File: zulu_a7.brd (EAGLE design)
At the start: 61 x 25.4 mm, 183 parts, among them J1 Pmod 2x6, Q1 12MHz 25ppm (FPGA + FT2232HQ), Q2 2N7002, Q3 MBT3904DW1T1, U1 XC7A35T-1CPG236C, U10 93LC46BT-I/SN, U2 FT2232HQ USB-UART/JTAG Bridge, U3 AS4C32M16SB-6TIN, U4 W25Q128JVSIQ, U8 LTC3569EUDC#TRPBF, X1 Molex 105017-0001 Micro-USB-B

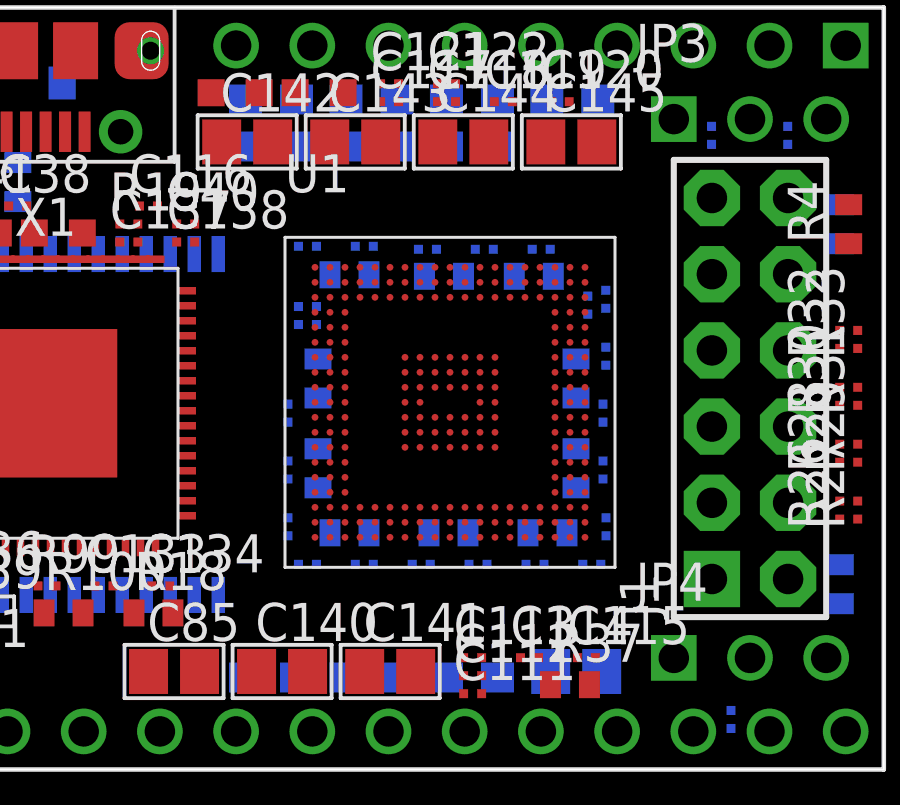
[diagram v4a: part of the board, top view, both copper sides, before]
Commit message: The BGA escape goes in: 1297 wires, 157 vias, DRC clean
First copper on the board. tools/escape.py --apply, run after make_board and
never before -- make_board rewrites <signals> empty, so regenerating from here
throws the escape away and this has to be re-run. That is intended: placement is
the source of truth and the escape is derived from it.

    stage 1  113 power and ground balls ganged on L1: 73 edges, 40 components
    stage 2  54 escapes drop through vias in the 2.00 mm moat
    stage 3  103 escapes leave the package to a fan-out ring at 7.260 mm
             half-width, 103 vias at 0.390 pitch using 40.170 of 58.080 mm

The escape CLOSES: all 47 enclosed ring-1 balls found a lane, every one outward
through ring 0, none needing to come inward through ring 2.

Not one via goes inside the ball field, and the arithmetic for that is worth
keeping in view: at a 0.225 land the four-ball void is 0.4821 across, and 0.090
of clearance leaves 0.3021 for a via land against the board's 0.300. It "fits"
by 0.0021 mm, which is a rounding error and not a fit.

check_board: 1297 wires and 157 vias across 175 signals, all copper on L1, every
wire and via clearing foreign copper by the full 0.090, every wire end landing on
its own net. 0 findings. 52 of 175 signals still carry no copper.

The docstring said stage 1 was all the file did. It has done all three for some
time; it now says so, and says what it does NOT do -- seven ganged components are
stranded (P2, B14, H18, V18 on GND, V6, V9, V11 on VCC3V3) and need a lane each
like a signal, which this pass does not draw.

Co-Authored-By: Claude Opus 5 <noreply@anthropic.com>
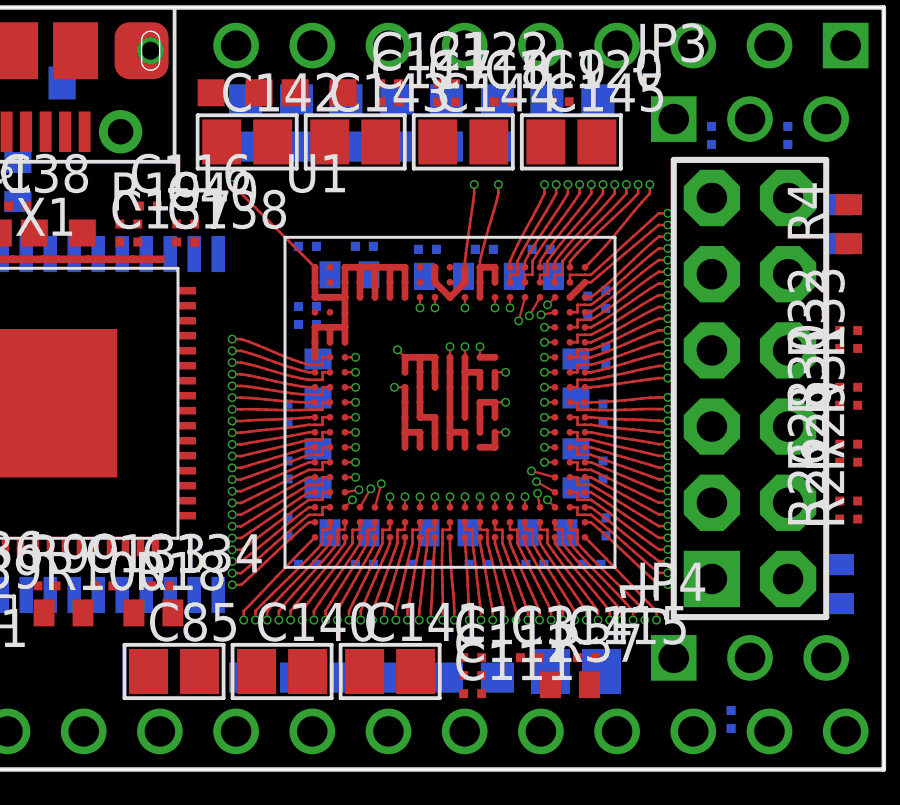
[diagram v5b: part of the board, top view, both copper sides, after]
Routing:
- net GND: track 0.00 -> 72.6 mm, vias 0 -> 19
- net VCC3V3: track 0.00 -> 33.5 mm, vias 0 -> 16
- net GNDADC: track 0.00 -> 4.84 mm, vias 0 -> 1
- net BS0: track 0.00 -> 4.43 mm, vias 0 -> 1
- net CHAN2: track 0.00 -> 4.36 mm, vias 0 -> 1
- net VCC1V0: track 0.00 -> 4.35 mm, vias 0 -> 1
- net CHAN0: track 0.00 -> 4.30 mm, vias 0 -> 1
- net CHAN15: track 0.00 -> 4.24 mm, vias 0 -> 1
- net RAS#: track 0.00 -> 4.24 mm, vias 0 -> 1
- net A0: track 0.00 -> 4.23 mm, vias 0 -> 1
- net JA1: track 0.00 -> 4.23 mm, vias 0 -> 1
- net FLASH-D00: track 0.00 -> 4.19 mm, vias 0 -> 1
- net UART_FT_CTS#: track 0.00 -> 4.17 mm, vias 0 -> 1
- net CHAN18: track 0.00 -> 4.07 mm, vias 0 -> 1
- net WE#: track 0.00 -> 4.06 mm, vias 0 -> 1
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
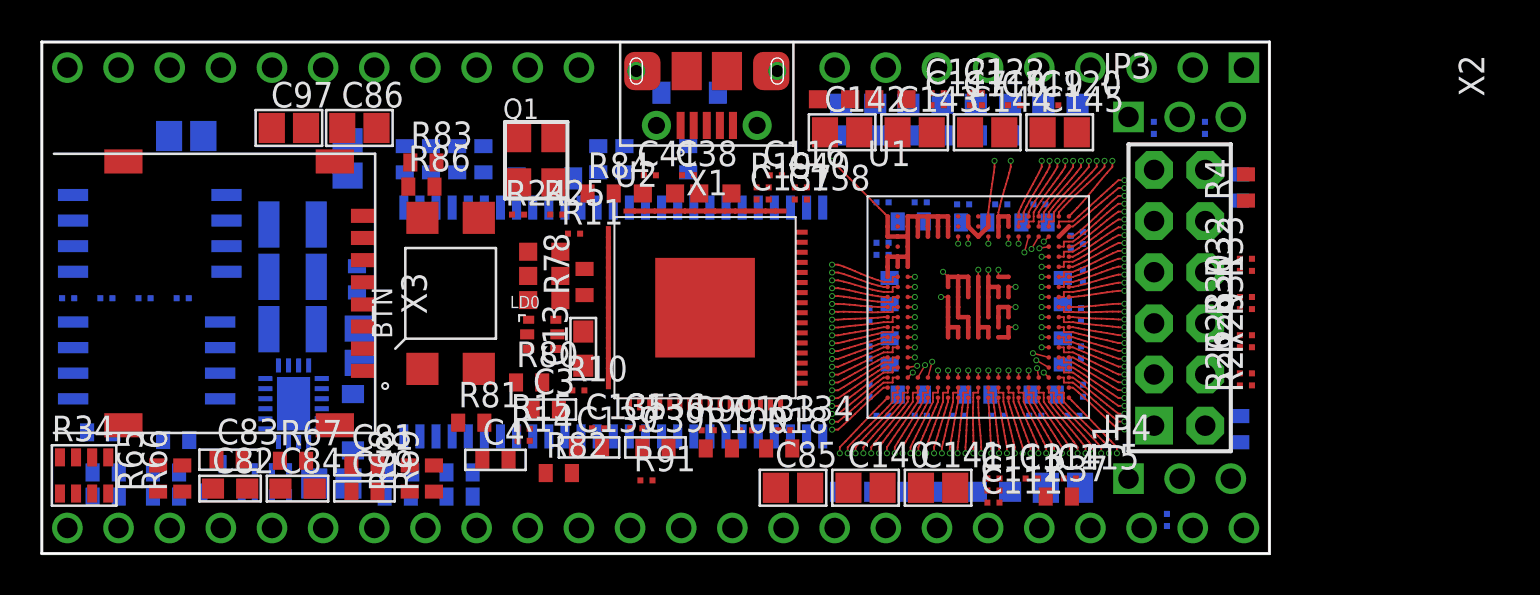
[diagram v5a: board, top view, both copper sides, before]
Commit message: Route 25 more signals: the missing QFN escape, the run order, and the nets nobody owned
52 signals carried no copper; 27 do now, and check_board is clean at 0
findings -- 2373 wires, 375 vias, everything clearing foreign copper by
>= 0.090 mm.

Most of the 52 were never attempted. signals.py had five group regexes and
the board is not only buses: the Pmod signals, the LEDs, the pushbutton, the
slide switches, the LTC3569 feedback dividers, PGOOD, MODE, the XADC pair,
the shared 12 MHz clock and the EEPROM data line matched none of them and
reported "unrouted" every run without a router ever looking at them.

escape_qfn.py was not in the chain. U2's QFN-64 fan-out is a stage of its
own; without it twenty signals converging on a 0.5 mm pitch each invented a
via mid-route in whatever order the router reached them. jtag goes 1/12 to
6/12 with it in -- the number its own header predicts.

make_board.py: reserve the fan corridor against parts on the routed rails.
RING guards the ring-via band and NOVIA the ball field, and the 2.10 mm
annulus between them is where stage 3 fans 1170 traces at 0.19 mm pitch. A
via needs 0.48 mm of clear width there and has 0.10. Six decoupling caps had
landed in it; four worked on luck, C95 needed a 3.45 mm stub and C96 could
not be reached at all. Signal parts stay -- they reach their ring via on L16
and need no new hole.

Ground now runs LAST, not straight after escape. Its stitching is
opportunistic and a through hole blocks every layer: 85 vias at 2.60 mm
pitch sealed the corridors VCC1V0 needed across the regulator corner and the
rail would not close. Run after power it places 78 and works around the
traces. Decisive for power.py; measured as noise for the signal groups
(SDRAM 29 of 39 against 28).

power.py: FT-VCORE/VPHY/VPLL and VU/VEXT/USB5V0 join RAILS. escape_qfn
declines power nets and signals.py caught the FT ones on "^FT-", so nothing
owned them. The three FT rails route. The three supply rails do not close
yet and are left her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
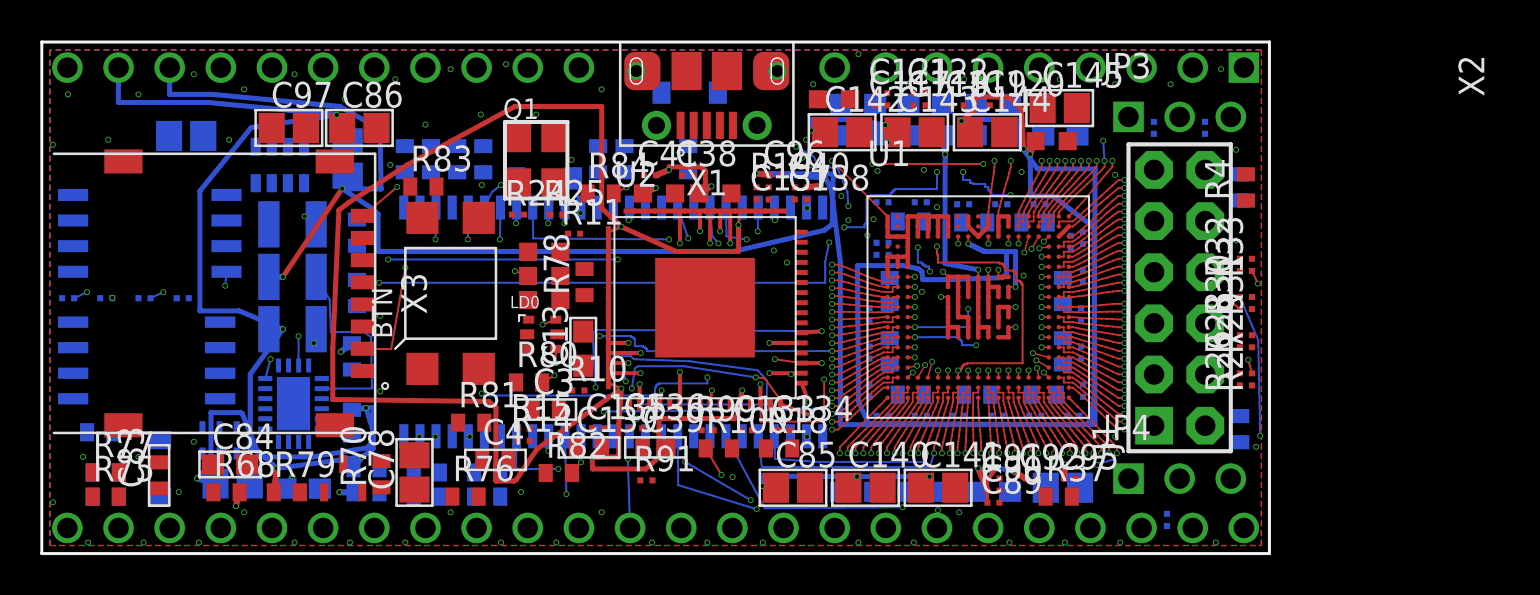
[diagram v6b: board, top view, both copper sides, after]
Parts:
- moved R34 19.1 mm to (12.6, 19.3), flipped to the bottom
- moved R76 17.9 mm to (21.0, 2.83), flipped to the top
- moved R75 17.6 mm to (3.17, 2.83), flipped to the top
- moved R77 17.6 mm to (3.17, 4.03), flipped to the top
- moved C96 17.5 mm to (36.4, 18.8), flipped to the top, turned to 0 degrees
- moved R69 16.3 mm to (3.17, 4.03), flipped to the bottom, turned to 0 degrees
- moved R71 16.0 mm to (19.1, 4.03)
- moved R73 16.0 mm to (22.1, 4.03)
- moved C89 15.9 mm to (47.3, 2.53), flipped to the top
- moved C116 15.6 mm to (51.7, 15.7), flipped to the bottom, turned to 90 degrees
- moved R66 15.2 mm to (22.1, 2.83), flipped to the bottom, turned to 0 degrees
- moved C90 14.8 mm to (47.3, 3.13), flipped to the top
- moved R72 14.6 mm to (3.17, 2.83)
- moved R74 12.8 mm to (19.1, 2.83)
- moved C109 12.0 mm to (41.1, 8.09)
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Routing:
- net VCC1V8: track 1.21 -> 221.6 mm, vias 2 -> 13
- net VCC1V0: track 4.35 -> 154.1 mm, vias 1 -> 18
- net CHAN20: track 3.91 -> 88.0 mm, vias 1 -> 8
- net FT-VCORE: track 0.00 -> 77.7 mm, vias 0 -> 6
- net CHAN27: track 4.05 -> 65.8 mm, vias 1 -> 2
- net CHAN11: track 0.35 -> 61.5 mm, vias 1 -> 8
- net CHAN19: track 3.09 -> 60.3 mm, vias 1 -> 5
- net SD-CLK: track 0.35 -> 44.8 mm, vias 1 -> 5
- net SD-DAT3: track 3.34 -> 45.2 mm, vias 1 -> 2
- net CHAN9: track 0.35 -> 41.8 mm, vias 1 -> 4
- net SD-DAT1: track 4.00 -> 41.9 mm, vias 1 -> 5
- net SW3_NET: track 0.00 -> 35.4 mm, vias 0 -> 2
- net A8: track 0.35 -> 33.9 mm, vias 1 -> 4
- net CHAN6: track 0.35 -> 31.9 mm
- net A12: track 0.35 -> 31.4 mm, vias 1 -> 4
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- added copper zone on layer 1, net GND
- added copper zone on layer 16, net GND
- added copper zone on layer 2, net GND
- added copper zone on layer 5, net VCC3V3

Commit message: signals.py: validate the finished greedy plan instead of trusting the run
The greedy router checked every route against `rivals` -- the plan AT THAT
INSTANT -- and never looked at the finished set. That check is correct when
it is made and stops being correct immediately: rip-up removes members and
adds others, the best-round snapshot can restore a net that was placed
before the net it now sits on, and pairplan is merged in at the end having
been routed against none of the group. PMOD-4 came out of it with its L3
trace through PMOD-7's via at -0.16 mm, a short between two Pmod signals
that only check_board.py could see.

The clearance test was never the problem. collides() is if anything
stricter than check_board -- it measures a wire against a via at
STUB_W/2 + VIA_L/2 + clr, 0.34 mm, because route[1] holds traces and stubs
together and carries no per-segment width. So the fix reuses it unchanged
and only changes WHEN it runs: a final pass over the completed plan that
rips up the worst offender until nothing conflicts, worst-first so one
selfish route cannot evict several good ones, sorted() so the result is
reproducible.

It rips up rather than re-routing on purpose. Re-routing inside that loop
would be checked against a plan the loop is still changing, which is the
original bug in a different hat; an airwire says "this run could not place
it", which is true.

On the current board it drops PMOD-7 and EE-CLK, and check_board is clean
with no hand editing -- 2365 wires, 374 vias, 0 findings, 27 of 175 signals
still bare, the same count the manual rip-up reached. EE-CLK is dropped by
the 0.34-against-0.29 margin above and check_board would have passed it:
that is the right way round for a guard, and it is the first thing to look
at if a net that should route keeps coming out as an airwire.

Co-Authored-By: Claude Opus 5 <noreply@anthropic.com>
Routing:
- net EE-CLK: track 30.7 -> 1.00 mm, vias 2 -> 1
- net PMOD-7: track 9.01 -> 0.00 mm, vias 1 -> 0
- net PMOD-4: track 0.00 -> 7.69 mm, vias 0 -> 1
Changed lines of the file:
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@@
 <contactref element="U1" pad="C17"/>
 </signal>
-<signal name="PMOD-4">
+<signal name="PMOD-4"><via x="60.44" y="11.4502" extent="1-16" drill="0.2" diameter="0.3"/><wire x1="60.44" y1="11.4502" x2="59.15" y2="12.5" width="0.1" layer="3"/><wire x1="59.15" y1="12.5" x2="59" y2="12.55" width="0.1" layer="3"/><wire x1="59" y1="12.55" x2="55.25" y2="12.55" width="0.1" layer="3"/><wire x1="55.25" y1="12.55" x2="55.23" y2="13.97" width="0.1" layer="3"/><wire x1="60.09" y1="10.844" x2="60.44" y2="11.4502" width="0.1" layer="1"/>
 <contactref element="J1" pad="4"/>
 <contactref element="R29" pad="2"/>
@@
 <contactref element="U1" pad="T17"/>
 </signal>
-<signal name="PMOD-7"><via x="58.9538" y="12.59" extent="1-16" drill="0.2" diameter="0.3"/><wire x1="58.9538" y1="12.59" x2="60.1" y2="12.6" width="0.1" layer="4"/><wire x1="60.1" y1="12.6" x2="60.15" y2="11.25" width="0.1" layer="4"/><wire x1="60.15" y1="11.25" x2="60.25" y2="9.5" width="0.1" layer="4"/><wire x1="60.25" y1="9.5" x2="59.5" y2="8.05" width="0.1" layer="4"/><wire x1="59.5" y1="8.05" x2="57.77" y2="6.35" width="0.1" layer="4"/><wire x1="59.49" y1="12.14" x2="58.9538" y2="12.59" width="0.1" layer="1"/>
+<signal name="PMOD-7">
 <contactref element="J1" pad="7"/>
 <contactref element="R30" pad="1"/>
@@
 <contactref element="U2" pad="63"/>
 </signal>
-<signal name="EE-CLK"><via x="3.5" y="12.7" extent="1-16" drill="0.2" diameter="0.3"/><wire x1="29.133" y1="9.458" x2="25.8" y2="8" width="0.1" layer="3"/><wire x1="25.8" y1="8" x2="21.95" y2="7.6" width="0.1" layer="3"/><wire x1="21.95" y1="7.6" x2="15" y2="10.3" width="0.1" layer="3"/><wire x1="15" y1="10.3" x2="12.15" y2="14.05" width="0.1" layer="3"/><wire x1="12.15" y1="14.05" x2="3.5" y2="14.05" width="0.1" layer="3"/><wire x1="3.5" y1="14.05" x2="3.5" y2="12.7" width="0.1" layer="3"/><wire x1="3.504" y1="12.68" x2="3.5" y2="12.7" width="0.1" layer="16"/><via x="29.133" y="9.458" extent="1-16" drill="0.2" diameter="0.3"/><wire x1="28.133" y1="9.458" x2="29.133" y2="9.458" width="0.2" layer="1"/>
+<signal name="EE-CLK"><via x="29.133" y="9.458" extent="1-16" drill="0.2" diameter="0.3"/><wire x1="28.133" y1="9.458" x2="29.133" y2="9.458" width="0.2" layer="1"/>
 <contactref element="R96" pad="1"/>
 <contactref element="U10" pad="2"/>
